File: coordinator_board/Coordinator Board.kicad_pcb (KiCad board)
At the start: 2 copper layers, 68.2 x 36.5 mm, 19 parts, among them P1 POWER, P10 Mounting Hole, P11 Mounting Hole, P12 Mounting Hole, P13 Mounting Hole, P3 Peripheral, P4 SERIAL, P5 PGRM, SW1 Switch_SPDT_x2, U1 LM3671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

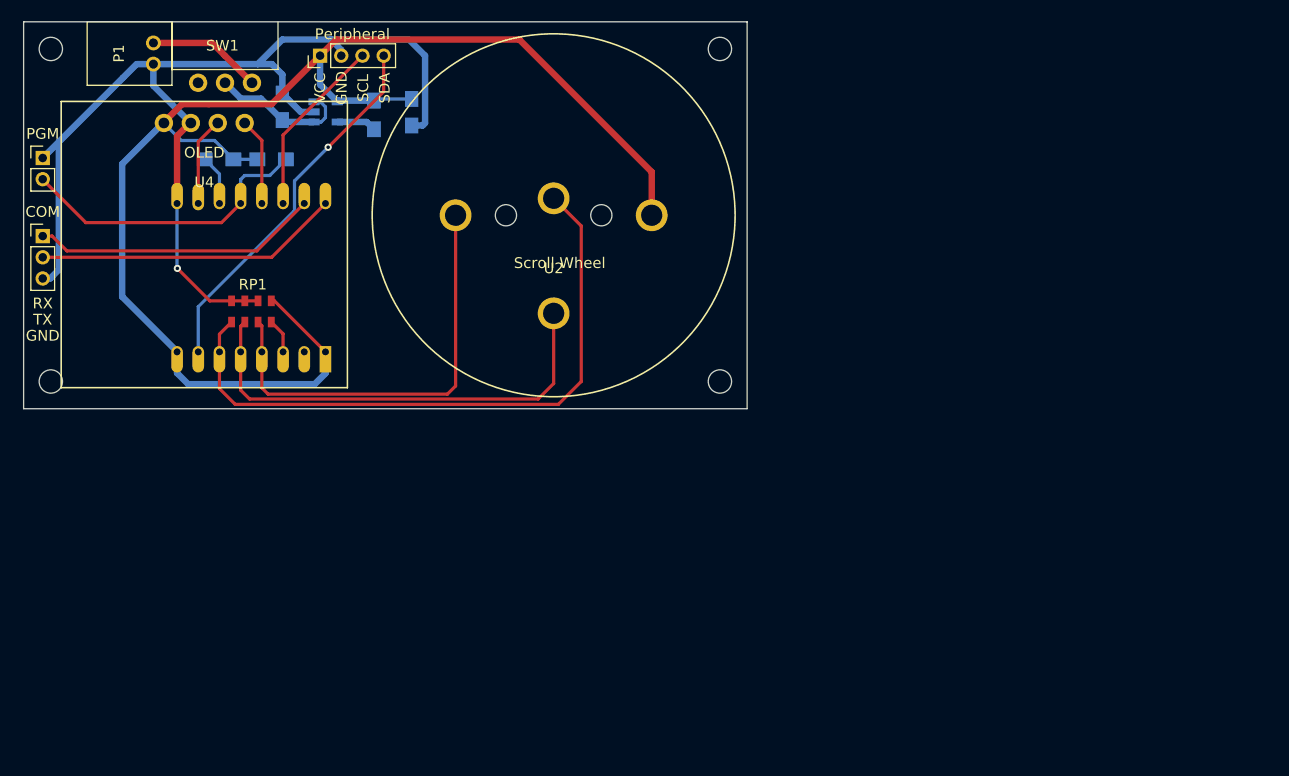
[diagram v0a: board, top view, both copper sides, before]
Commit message: Added rotary encoder footprint
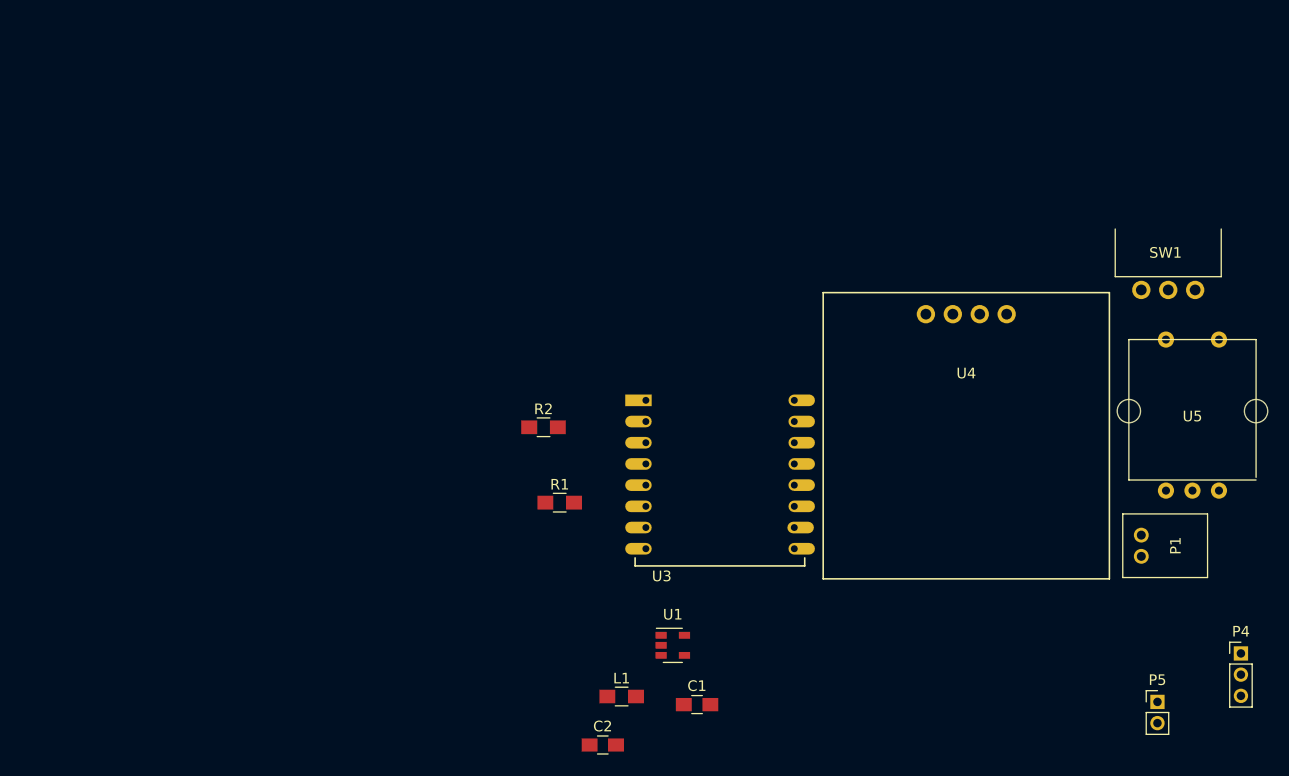
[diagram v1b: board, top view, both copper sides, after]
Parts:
- removed P10, P11, P12, P13: Mounting Hole, Mounting_Holes:MountingHole_2.2mm_M2
- removed P3: Peripheral, Pin_Headers:Pin_Header_Straight_1x04_Pitch2.00mm
- removed RP1: 10k, R_Array:R_Array_Concave_4x0805
- removed U2: TSWA-3N-CD23, TSWA:TSWA-3N-CD23
- added U5: Rotary_Encoder, Rotary_Encoder:Rotary_Encoder, F.Cu at (191.3, 109.5)
- C1, C2, L1, R1, R2, U1, U3: moved to F.Cu
- moved P4 119.7 mm to (195.8, 132.3)
- moved P5 117.0 mm to (188.0, 136.9)
- moved P1 104.1 mm to (186.4, 122.2), turned to 90 degrees
- moved SW1 91.1 mm to (189.0, 98.0)
- moved U4 74.1 mm to (169.9, 98.3)
- moved C1 68.6 mm to (144.5, 137.2), turned to 0 degrees
- moved C2 62.4 mm to (135.6, 141.0), turned to 0 degrees
- moved U1 60.0 mm to (142.2, 131.6)
- moved L1 59.6 mm to (137.4, 136.4), turned to 0 degrees
- moved R1 42.3 mm to (131.6, 118.1), turned to 0 degrees
- moved R2 39.7 mm to (130.0, 111.0)
- moved U3 30.6 mm to (139.7, 108.5), turned to 0 degrees
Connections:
- U3 pad 14: Net-(P3-Pad3) -> (no net)
- U3 pad 3: Net-(RP1-Pad4) -> (no net)
- U3 pad 7: Net-(P3-Pad4) -> (no net)
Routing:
- net Net-(C2-Pad1): track 132.6 -> 0.00 mm
- net Net-(C1-Pad2): track 103.6 -> 0.00 mm, vias 1 -> 0
- net Net-(U3-Pad6): track 60.7 -> 0.00 mm
- net Net-(U3-Pad5): track 43.7 -> 0.00 mm
- net Net-(U3-Pad4): track 41.3 -> 0.00 mm
- net Net-(P3-Pad4): track 35.2 -> 0.00 mm, vias 1 -> 0
- net Net-(P4-Pad2): track 28.8 -> 0.00 mm
- net Net-(P5-Pad2): track 28.4 -> 0.00 mm
- net Net-(P4-Pad1): track 27.1 -> 0.00 mm
- net Net-(P3-Pad3): track 17.0 -> 0.00 mm
- net Net-(C1-Pad1): track 13.5 -> 0.00 mm
- net Net-(P1-Pad1): track 10.9 -> 0.00 mm
- net Net-(U3-Pad10): track 8.38 -> 0.00 mm
- net Net-(U3-Pad13): track 8.32 -> 0.00 mm
- net Net-(R2-Pad1): track 4.73 -> 0.00 mm
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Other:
- board outline removed
- board text removed: "COM"
- board text removed: "ESP-12"
- board text removed: "GND"
- board text removed: "OLED"
- board text removed: "PGM"
- board text removed: "Peripheral"
- board text removed: "RX"
- board text removed: "Raver Lights Coordinator v2.0 Copyright Bryan Hughes 2016"
- board text removed: "SCL"
- board text removed: "SDA"
- board text removed: "Scroll Wheel"
- board text removed: "TX"
- board text removed: "VCC"

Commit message: Finished revision of coordinator board
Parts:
- added R3: 0, Resistors_SMD:R_0805_HandSoldering, F.Cu at (166.8, 111.8)
- added R4: 10k, Resistors_SMD:R_0805_HandSoldering, F.Cu at (160.8, 109.4)
- added R5: 10k, Resistors_SMD:R_0805_HandSoldering, F.Cu at (167.0, 118.4)
- added R6: 10k, Resistors_SMD:R_0805_HandSoldering, F.Cu at (172.0, 118.4)
- C1, C2, L1, U1, U3: moved to B.Cu
- R1: value 1k -> 10k
- R2: value 10k -> 1k
- moved SW1 39.7 mm to (156.0, 120.2), turned to 270 degrees
- moved C2 37.8 mm to (153.0, 107.4), turned to 180 degrees
- moved P1 37.6 mm to (153.2, 104.6), turned to 180 degrees
- moved R2 36.8 mm to (166.8, 109.8)
- moved U3 36.0 mm to (173.5, 120.9), turned to 90 degrees
- moved P4 32.7 mm to (188.0, 100.6), turned to 90 degrees
- moved R1 32.5 mm to (163.8, 113.8), turned to 180 degrees
- moved L1 31.5 mm to (156.0, 111.0), turned to 90 degrees
- moved U1 23.6 mm to (152.6, 110.4)
- moved C1 23.4 mm to (153.2, 115.4)
- moved P5 14.1 mm to (190.0, 123.0), turned to 270 degrees
- moved U5 2.40 mm to (190.0, 111.5)
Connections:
- net Net-(C1-Pad2) renamed GND
- C2 pad 1: Net-(C2-Pad1) -> +3V3
- L1 pad 2: Net-(C2-Pad1) -> +3V3
- R1 pad 1: Net-(P5-Pad2) -> +3V3
- R1 pad 2: Net-(C2-Pad1) -> Net-(R1-Pad2)
- R2 pad 1: Net-(R2-Pad1) -> Net-(P5-Pad2)
- R2 pad 2: Net-(C2-Pad1) -> Net-(R2-Pad2)
- U1 pad 4: Net-(C2-Pad1) -> +3V3
- U3 pad 1: Net-(C2-Pad1) -> Net-(R6-Pad2)
- U3 pad 10: Net-(U3-Pad10) -> Net-(R4-Pad1)
- U3 pad 11: Net-(R2-Pad1) -> Net-(R1-Pad2)
- U3 pad 14: (no net) -> Net-(U3-Pad14)
- U3 pad 3: (no net) -> Net-(R5-Pad1)
- U3 pad 8: Net-(C2-Pad1) -> +3V3
- U4 pad 1: Net-(C2-Pad1) -> +3V3
- U4 pad 3: Net-(U3-Pad10) -> Net-(U3-Pad14)
- U5 pad 1: Net-(U3-Pad5) -> Net-(U3-Pad4)
- U5 pad 3: Net-(U3-Pad4) -> Net-(U3-Pad5)
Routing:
- net GND: track 0.00 -> 87.4 mm
- net +3V3: track 0.00 -> 53.7 mm
- net Net-(P5-Pad2): track 0.00 -> 37.2 mm
- net Net-(U3-Pad6): track 0.00 -> 33.7 mm
- net Net-(U3-Pad5): track 0.00 -> 32.4 mm
- net Net-(U3-Pad4): track 0.00 -> 24.6 mm
- net Net-(P4-Pad2): track 0.00 -> 22.3 mm
- net Net-(P4-Pad1): track 0.00 -> 22.2 mm
- net Net-(C1-Pad1): track 0.00 -> 14.1 mm
- net Net-(P1-Pad1): track 0.00 -> 13.8 mm
- net Net-(U3-Pad13): track 0.00 -> 10.4 mm
- net Net-(R1-Pad2): track 0.00 -> 7.32 mm
- net Net-(U3-Pad14): track 0.00 -> 7.28 mm
- net Net-(R5-Pad1): track 0.00 -> 5.00 mm
- net Net-(R4-Pad1): track 0.00 -> 2.77 mm
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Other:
- board outline added: 47 x 27 mm
- board text added: "GND"
- board text added: "PGM"
- board text added: "RX"
- board text added: "Raver Lights Coordinator v2.5 Copyright Bryan Hughes 2017"
- board text added: "TX"
- board text added: "UART"

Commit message: Created v2.6 of the coordinator board
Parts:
- removed R3: 0, Resistors_SMD:R_0805_HandSoldering
- P5: value PGRM -> PROGRAM
- U5: value Rotary_Encoder -> SF303GJ26; footprint Rotary_Encoder:Rotary_Encoder -> SF303GJ26:SF303GJ26
- moved P5 5.93 mm to (184.9, 119.9), turned to 0 degrees
- moved P4 3.05 mm to (184.9, 100.7)
- moved U5 2.60 mm to (187.9, 109.9), turned to 45 degrees
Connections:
- R2 pad 2: Net-(R2-Pad2) -> +3V3
- U3 pad 7: (no net) -> Net-(U3-Pad7)
- U5 pad 2: GND -> (no net)
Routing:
- net Net-(U3-Pad7): track 0.00 -> 46.8 mm
- net Net-(U3-Pad6): track 33.7 -> 45.1 mm
- net Net-(U3-Pad4): track 24.6 -> 34.8 mm
- net Net-(P5-Pad2): track 37.2 -> 32.8 mm
- net Net-(P4-Pad2): track 22.3 -> 18.7 mm
- net +3V3: track 53.7 -> 57.3 mm
- net Net-(P4-Pad1): track 22.2 -> 19.1 mm
- net Net-(U3-Pad5): track 32.4 -> 34.7 mm
- net Net-(R2-Pad2): track 2.00 -> 0.00 mm
- net GND: track 87.4 -> 87.1 mm, vias 0 -> 1
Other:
- board size 47 x 27 mm -> 42.5 x 27 mm
- board text added: "Off"
- board text added: "Raver Lights Coordinator v2.6 Copyright Bryan Hughes 2017"
- board text removed: "Raver Lights Coordinator v2.5 Copyright Bryan Hughes 2017"

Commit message: v2.7 of the coordinator board
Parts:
- removed P5: PROGRAM, Pin_Headers:Pin_Header_Straight_1x02_Pitch2.00mm
- added R7: 0, Resistors_SMD:R_0805_HandSoldering, F.Cu at (188.2, 120.9)
- added R8: 0, Resistors_SMD:R_0805_HandSoldering, F.Cu at (185.2, 120.9)
- added RP1: 10k, R_Array:R_Array_Concave_4x0805, F.Cu at (187.9, 105.9)
- added SW2: Switch_DPST, KMR6:KMR641NG, F.Cu at (153.4, 109.9)
- moved U5 2.75 mm to (187.9, 112.7)
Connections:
- U3 pad 7: Net-(U3-Pad7) -> Net-(R7-Pad1)
- U5 pad 2: (no net) -> Net-(R8-Pad2)
- U5 pad 6: Net-(U3-Pad7) -> Net-(R7-Pad2)
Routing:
- net Net-(R7-Pad1): track 0.00 -> 49.4 mm, vias 0 -> 2
- net Net-(U3-Pad7): track 46.8 -> 0.00 mm
- net +3V3: track 57.3 -> 81.6 mm
- net GND: track 87.1 -> 76.2 mm
- net Net-(R7-Pad2): track 0.00 -> 9.54 mm
- net Net-(RP1-Pad2): track 34.7 -> 41.1 mm
- net Net-(R8-Pad2): track 0.00 -> 5.34 mm
- net Net-(R2-Pad1): track 32.8 -> 27.9 mm
- net Net-(RP1-Pad1): track 34.8 -> 36.5 mm
- net Net-(RP1-Pad3): track 45.1 -> 43.9 mm
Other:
- board text added: "BTN"
- board text added: "D"
- board text added: "Raver Lights Coordinator v2.7 Copyright Bryan Hughes 2017"
- board text removed: "Raver Lights Coordinator v2.6 Copyright Bryan Hughes 2017"
